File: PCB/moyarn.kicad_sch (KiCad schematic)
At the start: 11 parts, among them U1 WeAct_Buck_DCDC, U2 WeAct_USBPD_to_DC, U3 TMC2209_SILENTSTEPSTICK

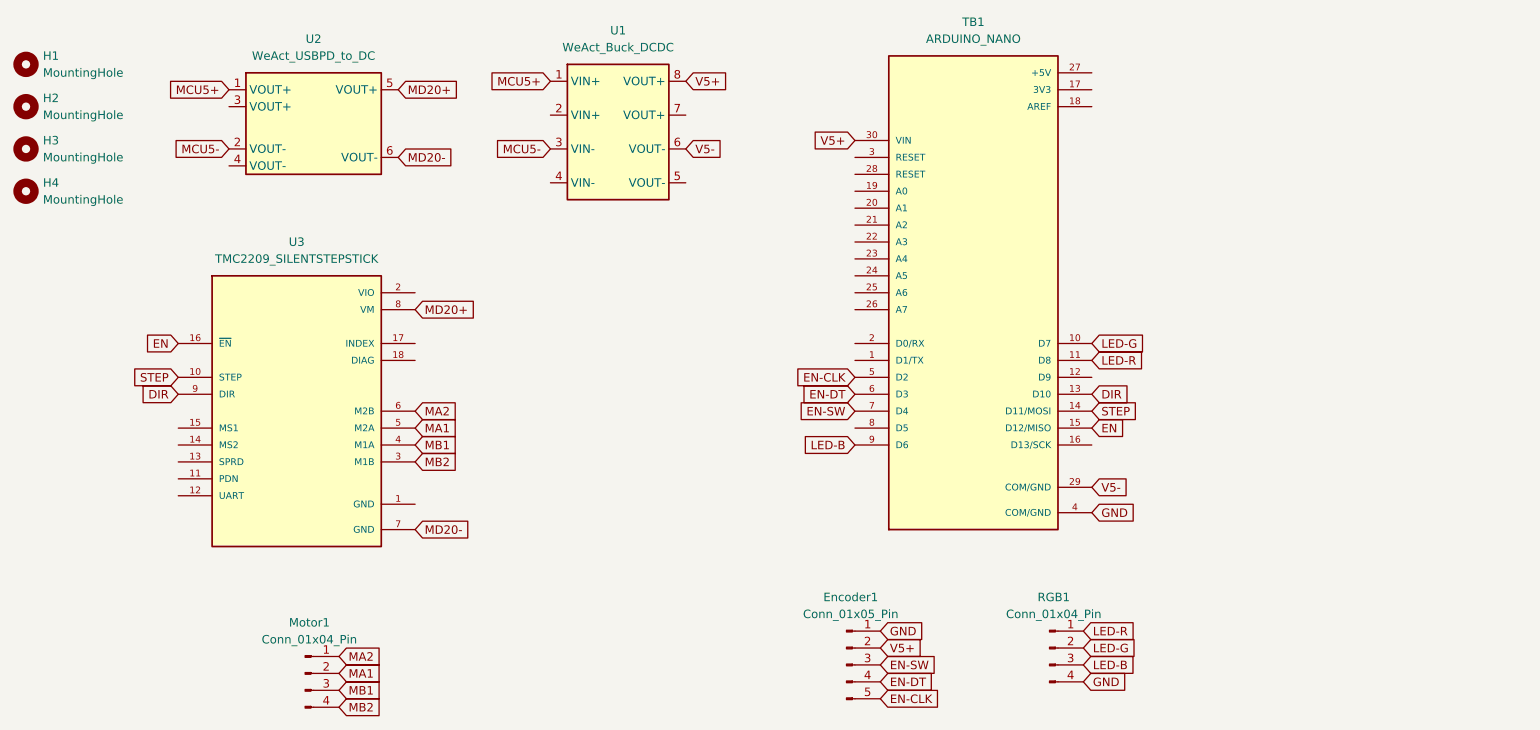
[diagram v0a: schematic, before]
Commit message: change arduino-nano to rp2040-zero
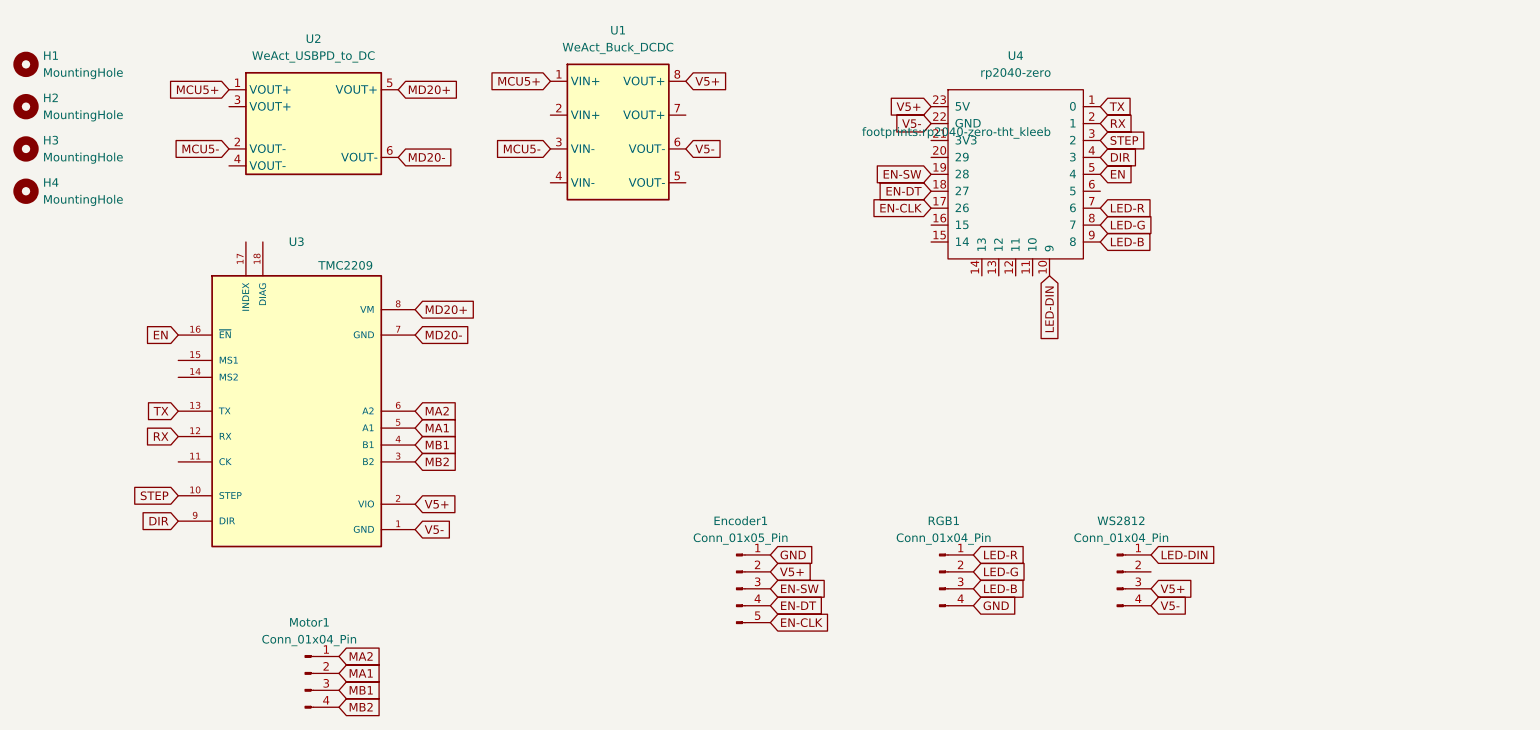
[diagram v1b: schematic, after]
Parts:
- removed TB1: ARDUINO_NANO, footprints:ARDUINO_NANO_snapeda, symbol ARDUINO_NANO_snapeda:ARDUINO_NANO
- added U4: rp2040-zero, footprints:rp2040-zero-tht_kleeb, symbol mcu_kleeb:rp2040-zero
- added WS2812: Conn_01x04_Pin, Connector_PinHeader_2.54mm:PinHeader_1x04_P2.54mm_Vertical, symbol Connector:Conn_01x04_Pin
- U3: value TMC2209_SILENTSTEPSTICK -> TMC2209
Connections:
- net DIR: now also U4.4 (3)
- net EN: now also U4.5 (4)
- net EN-CLK: now also U4.17 (26)
- net EN-DT: now also U4.18 (27)
- net EN-SW: now also U4.19 (28)
- net LED-B: now also U4.9 (8)
- net LED-G: now also U4.8 (7)
- net LED-R: now also U4.7 (6)
- net STEP: now also U4.3 (2)
- net V5+: now also U3.2 (VIO), U4.23 (5V), WS2812.3 (Pin_3)
- net V5-: now also U3.1 (GND), U4.22 (GND), WS2812.4 (Pin_4)
- net RX: now reaches U3.12 (RX)
- net RX: now also U4.2 (1)
- net TX: now reaches U3.13 (TX)
- net TX: now also U4.1 (0)
- new net LED-DIN: U4.10 (9), WS2812.1 (Pin_1)
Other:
- moved on the sheet: Encoder1, RGB1, U3

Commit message: pcb error mod and source mod
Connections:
- net GND is gone; now on net V5-: Encoder1.1 (Pin_1), RGB1.4 (Pin_4)
- net EN-CLK: now also U4.19 (28); no longer U4.17 (26)
- net EN-SW: now also U4.17 (26); no longer U4.19 (28)
- net LED-B: now also U4.7 (6); no longer U4.9 (8)
- net LED-R: now also U4.9 (8); no longer U4.7 (6)
